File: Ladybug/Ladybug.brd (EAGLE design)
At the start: 42.6 x 51 mm, 8 parts

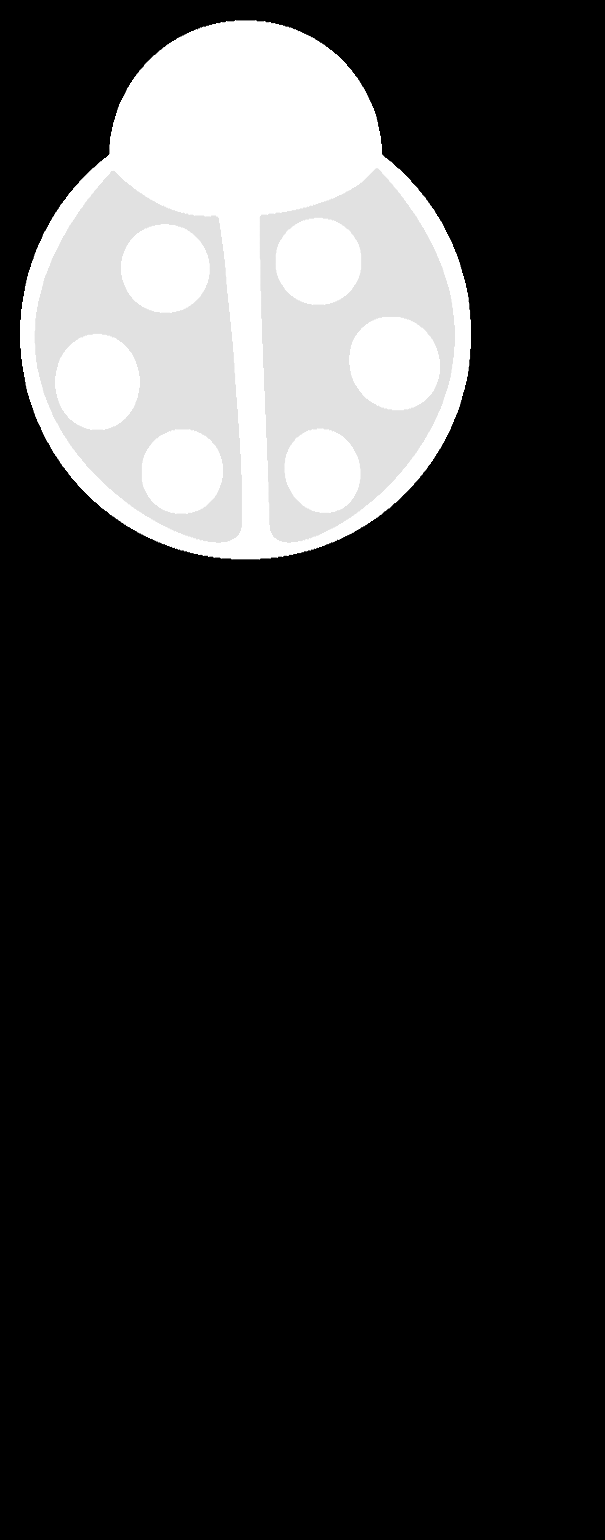
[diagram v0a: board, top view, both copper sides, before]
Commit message: Ladybug silkscreen use only one layer. Readded dimension layer.
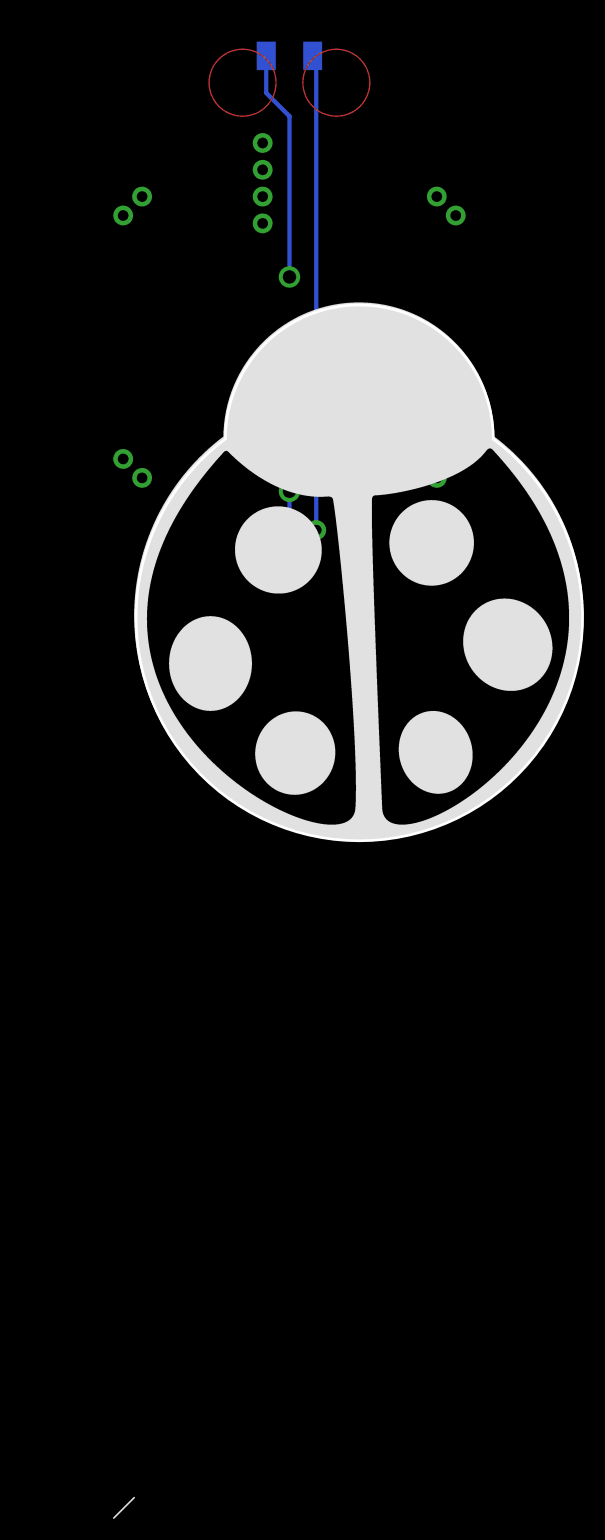
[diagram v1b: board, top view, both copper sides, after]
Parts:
- moved J1 4.24 mm to (27.9, 2.54)
- moved J2 4.24 mm to (11.4, 34.3)
- moved J5 4.24 mm to (11.4, 7.62)
- moved BATT 4.24 mm to (25.4, 6.35)
- moved J3 4.24 mm to (39.4, 34.3)
- moved J4 4.24 mm to (39.4, 7.62)
- moved J6 4.24 mm to (22.9, 31.8)
- moved R1 4.24 mm to (25.4, 47.6)
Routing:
- added copper zone on layer 1, net N$4
- added copper zone on layer 1, net N$5
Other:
- board size 42.6 x 51 mm -> 42.3 x 50.8 mm
